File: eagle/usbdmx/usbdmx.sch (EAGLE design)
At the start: 16 parts, among them IC1 MAX3468CSA, IC2 MAX3468CSA, Q1 16MHz

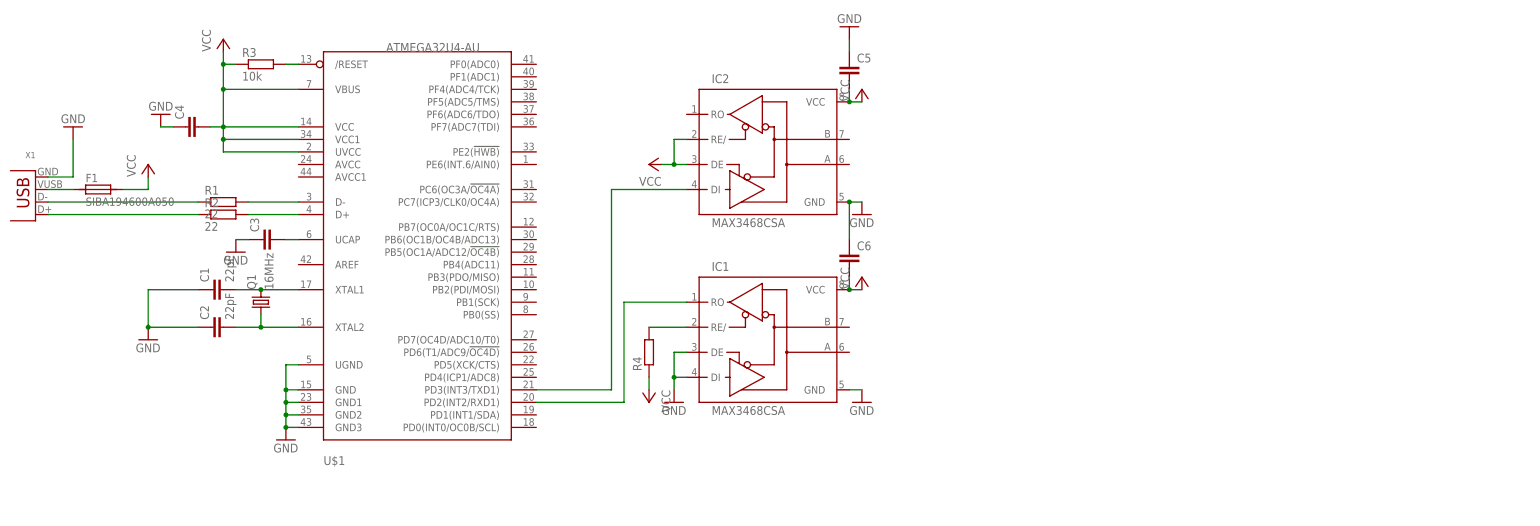
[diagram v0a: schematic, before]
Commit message: simple layout without galvanic isolation
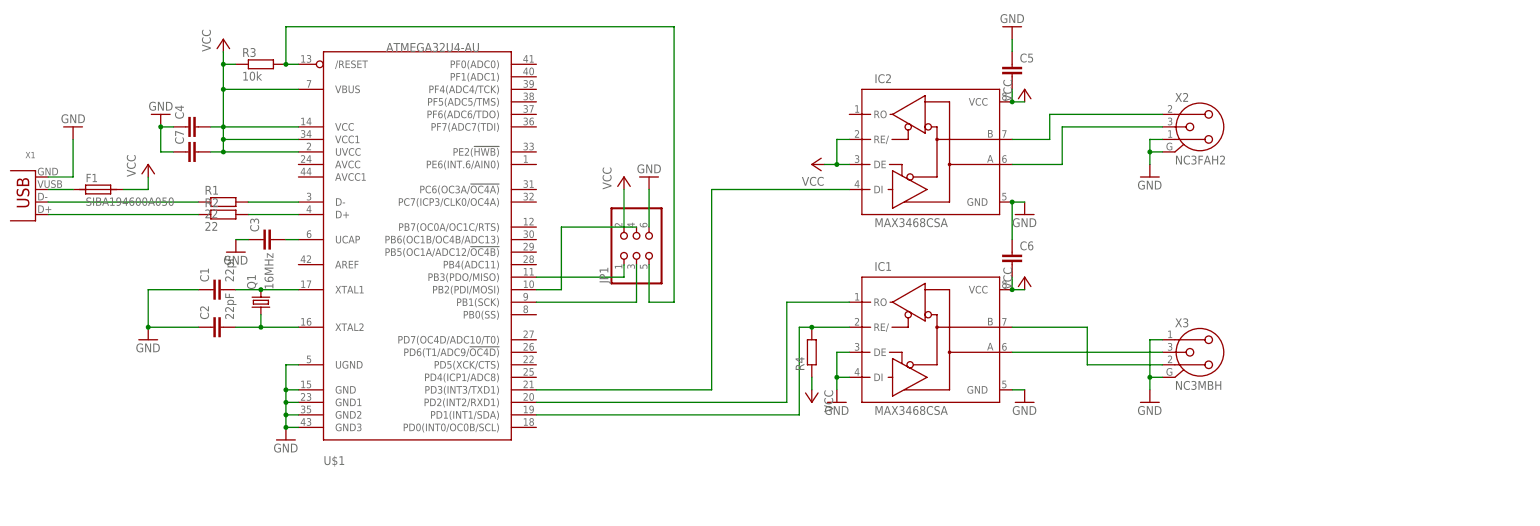
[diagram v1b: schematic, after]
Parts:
- added C7: (no value), rcl:C-EUC0805
- added JP1: (no value), pinhead:PINHD-2X3_2.54-SMD
- added X2: NC3FAH2, con-neutrik_ag:NC3FAH2
- added X3: NC3MBH, con-neutrik_ag:NC3MBH
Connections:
- new net N$13: JP1.1, U$1.PB3(PDO/MISO)
- new net N$14: JP1.4, U$1.PB2(PDI/MOSI)
- new net N$15: JP1.3, U$1.PB1(SCK)
- new net N$16: IC1.RE/, R4.2, U$1.PD1(INT1/SDA)
- new net N$17: IC2.B, X2.1
- new net N$18: IC1.A, X3.3
- new net N$19: IC1.B, X3.2
- net GND: now also C7.1, JP1.6, X2.2, X2.G, X3.1, X3.G
- net N$12: now also IC2.A, X2.3; no longer IC1.RE/, R4.2
- net N$9: now also JP1.5
- net VCC: now also C7.2, JP1.2
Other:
- moved on the sheet: C5, C6, IC1, IC2, R4

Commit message: complete design with optocouplers and dc-dc-transformer for galvanic isolation
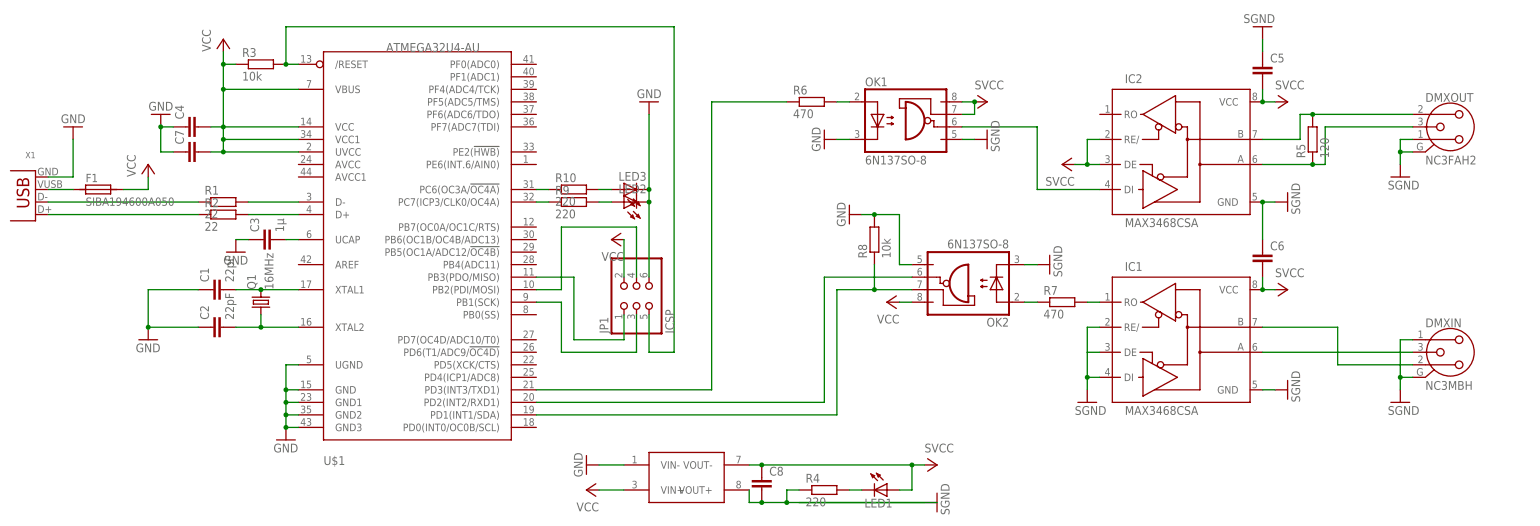
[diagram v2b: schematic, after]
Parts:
- removed X2: NC3FAH2, con-neutrik_ag:NC3FAH2
- removed X3: NC3MBH, con-neutrik_ag:NC3MBH
- added C8: (no value), rcl:C-EUC0805
- added DMXIN: NC3MBH, con-neutrik_ag:NC3MBH
- added DMXOUT: NC3FAH2, con-neutrik_ag:NC3FAH2
- added LED1, LED2, LED3: (no value), led:LEDSML0603
- added OK1, OK2: 6N137SO-8, optocoupler:6N137SO-8
- added R10, R9: 220, rcl:R-EU_R0805
- added R5: 120, rcl:R-EU_R0805
- added R6, R7: 470, rcl:R-EU_R0805
- added R8: 10k, rcl:R-EU_R0805
- added U$2: NTE0505SNTE0505MEC, murata-dcdc:NTE0505SNTE0505MEC
- C3: value (none) -> 1µ
- JP1: value (none) -> ICSP
- R4: value (none) -> 220
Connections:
- new net N$20: IC2.DI, OK1.VO
- new net N$21: IC1.RO, R7.2
- new net N$22: LED3.A, R10.2
- new net N$23: OK2.A, R7.1
- new net N$24: OK2.VO, U$1.PD2(INT2/RXD1)
- new net N$25: OK1.A, R6.2
- new net N$26: LED2.A, R9.2
- new net N$27: R9.1, U$1.PC7(ICP3/CLK0/OC4A)
- new net N$28: R10.1, U$1.PC6(OC3A/!OC4A)
- new net SGND: C5.1, C6.1, C8.2, DMXIN.1, DMXIN.G, DMXOUT.2, DMXOUT.G, IC1.DE, IC1.DI, IC1.GND, IC1.RE/, IC2.GND, OK1.GND, OK2.C, R4.1, U$2.VOUT+
- new net SVCC: C5.2, C6.2, C8.1, IC1.VCC, IC2.DE, IC2.RE/, IC2.VCC, LED1.A, OK1.VCC, OK1.VE, U$2.VOUT-
- net GND: now also LED2.C, LED3.C, OK1.C, OK2.GND, R8.2, U$2.VIN-; no longer C5.1, C6.1, IC1.DE, IC1.DI, IC1.GND, IC2.GND, X2.2, X2.G, X3.1, X3.G
- net N$10: now also R6.1; no longer IC2.DI
- net N$11: now also LED1.C, R4.2; no longer IC1.RO, U$1.PD2(INT2/RXD1)
- net N$12: now also DMXOUT.3, R5.1; no longer X2.3
- net N$16: now also OK2.VE, R8.1; no longer IC1.RE/, R4.2
- net N$17: now also DMXOUT.1, R5.2; no longer X2.1
- net N$18: now also DMXIN.3; no longer X3.3
- net N$19: now also DMXIN.2; no longer X3.2
- net VCC: now also OK2.VCC, U$2.VIN+; no longer C5.2, C6.2, IC1.VCC, IC2.DE, IC2.RE/, IC2.VCC, R4.1
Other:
- moved on the sheet: C5, C6, IC1, IC2, JP1, R4

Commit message: fix minor errors
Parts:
- C4, C5, C6, C7: value (none) -> 100n
- C8: value (none) -> 4,7µ
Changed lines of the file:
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@@
 <part name="GND6" library="supply1" deviceset="GND" device=""/>
 <part name="R3" library="rcl" deviceset="R-EU_" device="R0805" value="10k"/>
-<part name="C4" library="rcl" deviceset="C-EU" device="C0805"/>
+<part name="C4" library="rcl" deviceset="C-EU" device="C0805" value="100n"/>
 <part name="GND7" library="supply1" deviceset="GND" device=""/>
-<part name="C5" library="rcl" deviceset="C-EU" device="C0805"/>
-<part name="C6" library="rcl" deviceset="C-EU" device="C0805"/>
+<part name="C5" library="rcl" deviceset="C-EU" device="C0805" value="100n"/>
+<part name="C6" library="rcl" deviceset="C-EU" device="C0805" value="100n"/>
 <part name="JP1" library="pinhead" deviceset="PINHD-2X3" device="_2.54-SMD" value="ICSP"/>
 <part name="GND10" library="supply1" deviceset="GND" device=""/>
 <part name="P+7" library="supply1" deviceset="VCC" device=""/>
-<part name="C7" library="rcl" deviceset="C-EU" device="C0805"/>
+<part name="C7" library="rcl" deviceset="C-EU" device="C0805" value="100n"/>
 <part name="DMXOUT" library="con-neutrik_ag" deviceset="NC3" device="FAH2"/>
 <part name="DMXIN" library="con-neutrik_ag" deviceset="NC3" device="MBH"/>
@@
 <part name="SGND4" library="supply1" deviceset="GND" device="" value="SGND"/>
 <part name="SGND5" library="supply1" deviceset="GND" device="" value="SGND"/>
-<part name="C8" library="rcl" deviceset="C-EU" device="C0805"/>
+<part name="C8" library="rcl" deviceset="C-EU" device="C0805" value="4,7µ"/>
 <part name="SGND6" library="supply1" deviceset="GND" device="" value="SGND"/>
 <part name="R5" library="rcl" deviceset="R-EU_" device="R0805" value="120"/>
@@
 <pinref part="SGND3" gate="1" pin="GND"/>
 <wire x1="213.36" y1="33.02" x2="210.82" y2="33.02" width="0.1524" layer="91"/>
-<wire x1="210.82" y1="33.02" x2="210.82" y2="38.1" width="0.1524" layer="91"/>
 <pinref part="IC1" gate="G$1" pin="RE/"/>
 <wire x1="213.36" y1="38.1" x2="210.82" y2="38.1" width="0.1524" layer="91"/>
+<wire x1="210.82" y1="38.1" x2="210.82" y2="33.02" width="0.1524" layer="91"/>
+<junction x="210.82" y="33.02"/>
 </segment>
 <segment>
@@
 </segment>
 <segment>
+<pinref part="C5" gate="G$1" pin="1"/>
+<pinref part="SGND6" gate="1" pin="GND"/>
+<wire x1="246.38" y1="93.98" x2="246.38" y2="96.52" width="0.1524" layer="91"/>
+</segment>
+<segment>
+<pinref part="SGND7" gate="1" pin="GND"/>
+<pinref part="OK1" gate="A" pin="GND"/>
+<wire x1="187.96" y1="76.2" x2="185.42" y2="76.2" width="0.1524" layer="91"/>
+</segment>
+<segment>
+<pinref part="OK2" gate="A" pin="C"/>
+<pinref part="SGND8" gate="1" pin="GND"/>
+<wire x1="198.12" y1="50.8" x2="200.66" y2="50.8" width="0.1524" layer="91"/>
+</segment>
+<segment>
 <pinref part="U$2" gate="G$1" pin="VOUT+"/>
 <wire x1="142.24" y1="5.08" x2="142.24" y2="2.54" width="0.1524" layer="91"/>
@@
 <wire x1="144.78" y1="2.54" x2="149.86" y2="2.54" width="0.1524" layer="91"/>
 <junction x="144.78" y="2.54"/>
-<pinref part="SGND" gate="1" pin="GND"/>
-<wire x1="149.86" y1="2.54" x2="152.4" y2="2.54" width="0.1524" layer="91"/>
-<wire x1="152.4" y1="2.54" x2="177.8" y2="2.54" width="0.1524" layer="91"/>
 <wire x1="149.86" y1="2.54" x2="149.86" y2="5.08" width="0.1524" layer="91"/>
-<junction x="149.86" y="2.54"/>
 <pinref part="R4" gate="G$1" pin="1"/>
 <wire x1="149.86" y1="5.08" x2="152.4" y2="5.08" width="0.1524" layer="91"/>
-<wire x1="152.4" y1="2.54" x2="180.34" y2="2.54" width="0.1524" layer="91"/>
-</segment>
-<segment>
-<pinref part="C5" gate="G$1" pin="1"/>
-<pinref part="SGND6" gate="1" pin="GND"/>
-<wire x1="246.38" y1="93.98" x2="246.38" y2="96.52" width="0.1524" layer="91"/>
-</segment>
-<segment>
-<pinref part="SGND7" gate="1" pin="GND"/>
-<pinref part="OK1" gate="A" pin="GND"/>
-<wire x1="187.96" y1="76.2" x2="185.42" y2="76.2" width="0.1524" layer="91"/>
-</segment>
-<segment>
-<pinref part="OK2" gate="A" pin="C"/>
-<pinref part="SGND8" gate="1" pin="GND"/>
-<wire x1="198.12" y1="50.8" x2="200.66" y2="50.8" width="0.1524" layer="91"/>
+<pinref part="SGND" gate="1" pin="GND"/>
+<wire x1="149.86" y1="2.54" x2="177.8" y2="2.54" width="0.1524" layer="91"/>
+<junction x="149.86" y="2.54"/>
 </segment>
 </net>
@@
 </sheet>
 </sheets>
+<errors>
+</errors>
 </schematic>
 </drawing>

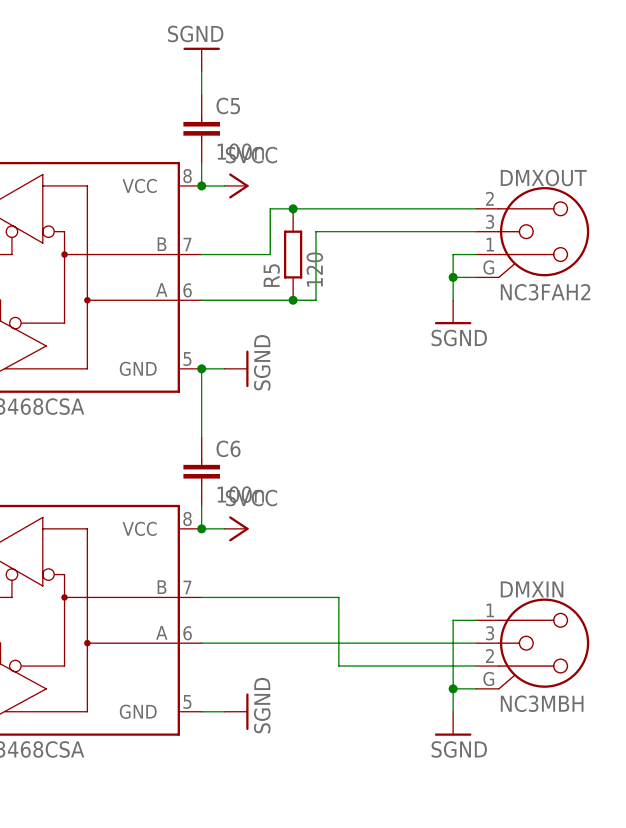
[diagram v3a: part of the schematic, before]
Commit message: invert outputs due to optocoupler
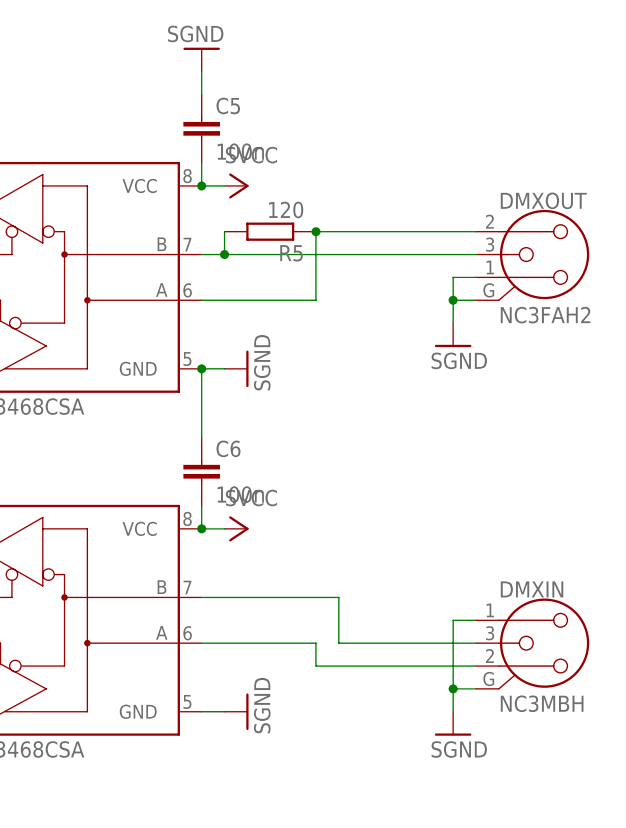
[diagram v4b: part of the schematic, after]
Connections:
- removed net N$19: DMXIN.2, IC1.B
- new net N$29: DMXIN.3, IC1.B
- net N$12: now also DMXOUT.1; no longer DMXOUT.3
- net N$17: now also DMXOUT.3; no longer DMXOUT.1
- net N$18: now also DMXIN.2; no longer DMXIN.3
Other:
- moved on the sheet: DMXOUT, R5
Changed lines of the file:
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@@
 <instance part="P+7" gate="VCC" x="114.3" y="55.88" rot="R90"/>
 <instance part="C7" gate="G$1" x="27.94" y="73.66" rot="R90"/>
-<instance part="DMXOUT" gate="G$1" x="284.48" y="78.74"/>
+<instance part="DMXOUT" gate="G$1" x="284.48" y="76.2"/>
 <instance part="DMXIN" gate="G$1" x="284.48" y="33.02"/>
 <instance part="U$2" gate="G$1" x="129.54" y="7.62"/>
@@
 <instance part="P+6" gate="VCC" x="251.46" y="83.82" rot="R270"/>
 <instance part="SGND4" gate="1" x="251.46" y="63.5" rot="R90"/>
-<instance part="SGND5" gate="1" x="274.32" y="68.58"/>
+<instance part="SGND5" gate="1" x="274.32" y="66.04"/>
 <instance part="C8" gate="G$1" x="144.78" y="7.62"/>
 <instance part="SGND6" gate="1" x="246.38" y="99.06" rot="R180"/>
-<instance part="R5" gate="G$1" x="256.54" y="76.2" rot="R90"/>
+<instance part="R5" gate="G$1" x="254" y="78.74" rot="R180"/>
 <instance part="OK1" gate="A" x="175.26" y="78.74"/>
 <instance part="OK2" gate="A" x="185.42" y="48.26" rot="R180"/>
@@
 <net name="N$17" class="0">
 <segment>
-<pinref part="DMXOUT" gate="G$1" pin="1"/>
-<wire x1="254" y1="81.28" x2="256.54" y2="81.28" width="0.1524" layer="91"/>
+<pinref part="IC2" gate="G$1" pin="B"/>
+<pinref part="DMXOUT" gate="G$1" pin="3"/>
+<wire x1="246.38" y1="76.2" x2="248.92" y2="76.2" width="0.1524" layer="91"/>
 <pinref part="R5" gate="G$1" pin="2"/>
-<wire x1="256.54" y1="81.28" x2="276.86" y2="81.28" width="0.1524" layer="91"/>
-<junction x="256.54" y="81.28"/>
-<pinref part="IC2" gate="G$1" pin="B"/>
-<wire x1="246.38" y1="76.2" x2="254" y2="76.2" width="0.1524" layer="91"/>
-<wire x1="254" y1="76.2" x2="254" y2="81.28" width="0.1524" layer="91"/>
-</segment>
-</net>
-<net name="N$18" class="0">
-<segment>
-<pinref part="DMXIN" gate="G$1" pin="3"/>
-<pinref part="IC1" gate="G$1" pin="A"/>
-<wire x1="276.86" y1="33.02" x2="246.38" y2="33.02" width="0.1524" layer="91"/>
-</segment>
-</net>
-<net name="N$19" class="0">
-<segment>
-<pinref part="IC1" gate="G$1" pin="B"/>
-<wire x1="246.38" y1="38.1" x2="261.62" y2="38.1" width="0.1524" layer="91"/>
-<wire x1="261.62" y1="38.1" x2="261.62" y2="30.48" width="0.1524" layer="91"/>
-<pinref part="DMXIN" gate="G$1" pin="2"/>
-<wire x1="261.62" y1="30.48" x2="276.86" y2="30.48" width="0.1524" layer="91"/>
+<wire x1="248.92" y1="76.2" x2="276.86" y2="76.2" width="0.1524" layer="91"/>
+<wire x1="248.92" y1="78.74" x2="248.92" y2="76.2" width="0.1524" layer="91"/>
+<junction x="248.92" y="76.2"/>
 </segment>
 </net>
@@
 </segment>
 <segment>
+<wire x1="274.32" y1="68.58" x2="274.32" y2="71.12" width="0.1524" layer="91"/>
+<pinref part="DMXOUT" gate="G$1" pin="2"/>
 <wire x1="274.32" y1="71.12" x2="274.32" y2="73.66" width="0.1524" layer="91"/>
-<pinref part="DMXOUT" gate="G$1" pin="2"/>
-<wire x1="274.32" y1="73.66" x2="274.32" y2="76.2" width="0.1524" layer="91"/>
-<wire x1="274.32" y1="76.2" x2="276.86" y2="76.2" width="0.1524" layer="91"/>
+<wire x1="274.32" y1="73.66" x2="276.86" y2="73.66" width="0.1524" layer="91"/>
 <pinref part="DMXOUT" gate="G$1" pin="G"/>
-<wire x1="276.86" y1="73.66" x2="274.32" y2="73.66" width="0.1524" layer="91"/>
-<junction x="274.32" y="73.66"/>
+<wire x1="276.86" y1="71.12" x2="274.32" y2="71.12" width="0.1524" layer="91"/>
+<junction x="274.32" y="71.12"/>
 <pinref part="SGND5" gate="1" pin="GND"/>
 </segment>
@@
 <net name="N$12" class="0">
 <segment>
+<wire x1="259.08" y1="71.12" x2="259.08" y2="78.74" width="0.1524" layer="91"/>
+<pinref part="DMXOUT" gate="G$1" pin="1"/>
+<wire x1="259.08" y1="78.74" x2="276.86" y2="78.74" width="0.1524" layer="91"/>
 <pinref part="IC2" gate="G$1" pin="A"/>
+<wire x1="259.08" y1="71.12" x2="246.38" y2="71.12" width="0.1524" layer="91"/>
 <pinref part="R5" gate="G$1" pin="1"/>
-<wire x1="246.38" y1="71.12" x2="256.54" y2="71.12" width="0.1524" layer="91"/>
-<wire x1="256.54" y1="71.12" x2="259.08" y2="71.12" width="0.1524" layer="91"/>
-<wire x1="259.08" y1="71.12" x2="259.08" y2="78.74" width="0.1524" layer="91"/>
-<junction x="256.54" y="71.12"/>
-<pinref part="DMXOUT" gate="G$1" pin="3"/>
-<wire x1="259.08" y1="78.74" x2="276.86" y2="78.74" width="0.1524" layer="91"/>
+<junction x="259.08" y="78.74"/>
 </segment>
 </net>
@@
 </segment>
 </net>
+<net name="N$29" class="0">
+<segment>
+<pinref part="IC1" gate="G$1" pin="B"/>
+<wire x1="246.38" y1="38.1" x2="261.62" y2="38.1" width="0.1524" layer="91"/>
+<wire x1="261.62" y1="38.1" x2="261.62" y2="33.02" width="0.1524" layer="91"/>
+<pinref part="DMXIN" gate="G$1" pin="3"/>
+<wire x1="261.62" y1="33.02" x2="276.86" y2="33.02" width="0.1524" layer="91"/>
+</segment>
+</net>
+<net name="N$18" class="0">
+<segment>
+<pinref part="DMXIN" gate="G$1" pin="2"/>
+<wire x1="276.86" y1="30.48" x2="259.08" y2="30.48" width="0.1524" layer="91"/>
+<wire x1="259.08" y1="30.48" x2="259.08" y2="33.02" width="0.1524" layer="91"/>
+<pinref part="IC1" gate="G$1" pin="A"/>
+<wire x1="259.08" y1="33.02" x2="246.38" y2="33.02" width="0.1524" layer="91"/>
+</segment>
+</net>

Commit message: replace the optocoupler package
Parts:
- OK1, OK2: value 6N137SO-8 -> 6N137SMD-8; device optocoupler:6N137SO-8 -> optocoupler:6N137SMD-8
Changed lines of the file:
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@@
 <part name="SGND6" library="supply1" deviceset="GND" device="" value="SGND"/>
 <part name="R5" library="rcl" deviceset="R-EU_" device="R0805" value="120"/>
-<part name="OK1" library="optocoupler" deviceset="6N137" device="SO-8"/>
-<part name="OK2" library="optocoupler" deviceset="6N137" device="SO-8"/>
+<part name="OK1" library="optocoupler" deviceset="6N137" device="SMD-8" value="6N137SMD-8"/>
+<part name="OK2" library="optocoupler" deviceset="6N137" device="SMD-8" value="6N137SMD-8"/>
 <part name="P+10" library="supply1" deviceset="VCC" device="" value="SVCC"/>
 <part name="SGND7" library="supply1" deviceset="GND" device="" value="SGND"/>

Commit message: add a solder pad to enable the boot loader
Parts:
- added SJ1: (no value), jumper:SJ
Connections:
- new net N$19: SJ1.2, U$1.PE2(!HWB)
- net GND: now also SJ1.1
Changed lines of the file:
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@@
 <part name="LED2" library="led" deviceset="LED" device="SML0603"/>
 <part name="LED3" library="led" deviceset="LED" device="SML0603"/>
+<part name="GND8" library="supply1" deviceset="GND" device=""/>
+<part name="SJ1" library="jumper" deviceset="SJ" device=""/>
 </parts>
 <sheets>
@@
 <instance part="LED2" gate="G$1" x="116.84" y="63.5" rot="R90"/>
 <instance part="LED3" gate="G$1" x="116.84" y="66.04" rot="R90"/>
+<instance part="GND8" gate="1" x="116.84" y="73.66" rot="R90"/>
+<instance part="SJ1" gate="1" x="106.68" y="73.66" rot="R180"/>
 </instances>
 <busses>
@@
 <wire x1="167.64" y1="60.96" x2="165.1" y2="60.96" width="0.1524" layer="91"/>
 <junction x="167.64" y="60.96"/>
+</segment>
+<segment>
+<pinref part="SJ1" gate="1" pin="1"/>
+<pinref part="GND8" gate="1" pin="GND"/>
+<wire x1="111.76" y1="73.66" x2="114.3" y2="73.66" width="0.1524" layer="91"/>
 </segment>
 </net>
@@
 </segment>
 </net>
+<net name="N$19" class="0">
+<segment>
+<pinref part="U$1" gate="G$1" pin="PE2(!HWB)"/>
+<pinref part="SJ1" gate="1" pin="2"/>
+<wire x1="99.06" y1="73.66" x2="101.6" y2="73.66" width="0.1524" layer="91"/>
+</segment>
+</net>
